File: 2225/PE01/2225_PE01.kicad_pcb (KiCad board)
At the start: 2 copper layers, 200 x 60 mm, 95 parts

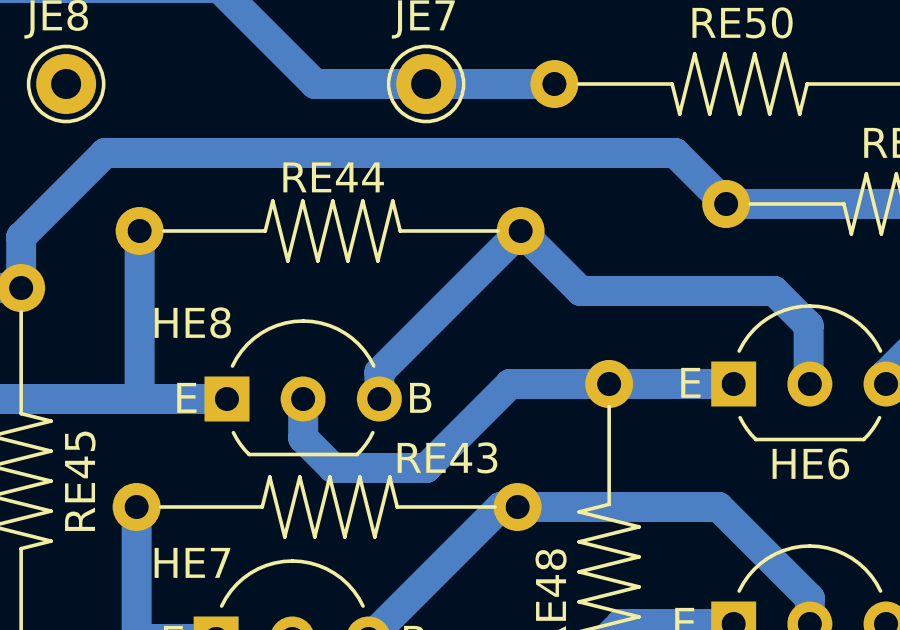
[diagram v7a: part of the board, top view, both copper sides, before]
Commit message: Re-routed a trace
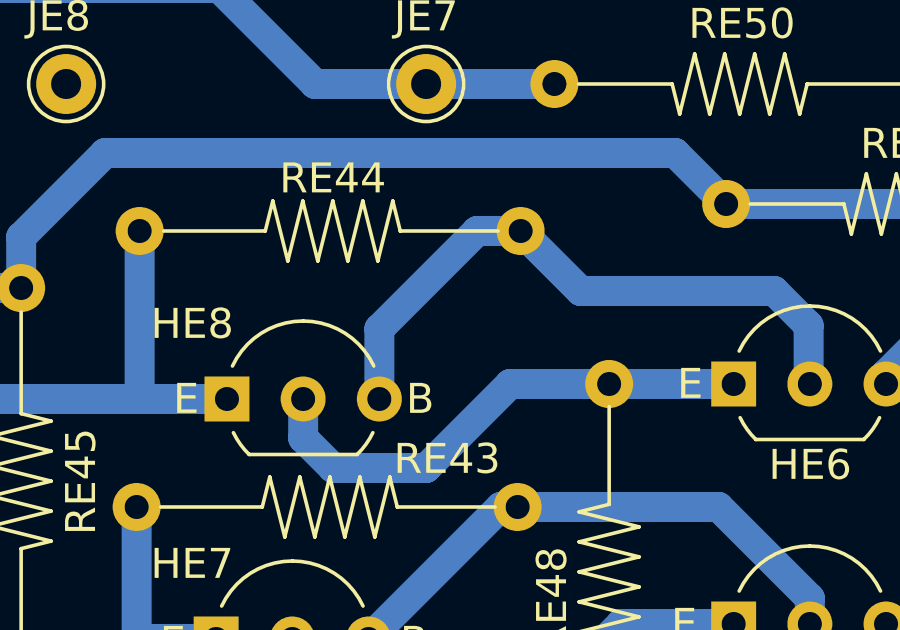
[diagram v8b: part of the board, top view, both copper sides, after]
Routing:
- net Net-(HE6-Pad2): track 20.4 -> 21.3 mm
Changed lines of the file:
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@@
   (segment (start 26.4 17.3) (end 26.4 16) (width 1) (layer "B.Cu") (net 31))
   (segment (start 35.65 12.4) (end 36.2 12.4) (width 1) (layer "B.Cu") (net 32))
-  (segment (start 28.94 16) (end 28.94 15.11) (width 1) (layer "B.Cu") (net 32))
+  (segment (start 32.2 10.4) (end 33.65 10.4) (width 1) (layer "B.Cu") (net 32))
+  (segment (start 28.94 13.66) (end 32.2 10.4) (width 1) (layer "B.Cu") (net 32))
+  (segment (start 28.94 16) (end 28.94 13.66) (width 1) (layer "B.Cu") (net 32))
   (segment (start 33.65 10.4) (end 35.65 12.4) (width 1) (layer "B.Cu") (net 32))
   (segment (start 42.1 12.4) (end 36.2 12.4) (width 1) (layer "B.Cu") (net 32))
   (segment (start 43.25 13.55) (end 42.1 12.4) (width 1) (layer "B.Cu") (net 32))
   (segment (start 43.25 15.5) (end 43.25 13.55) (width 1) (layer "B.Cu") (net 32))
-  (segment (start 28.94 15.11) (end 33.65 10.4) (width 1) (layer "B.Cu") (net 32))
   (segment (start 28.95 16) (end 28.94 16) (width 1) (layer "B.Cu") (net 32))
   (segment (start 173.5 6) (end 173.5 10) (width 3) (layer "B.Cu") (net 33))
